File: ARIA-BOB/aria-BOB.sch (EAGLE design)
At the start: 14 parts

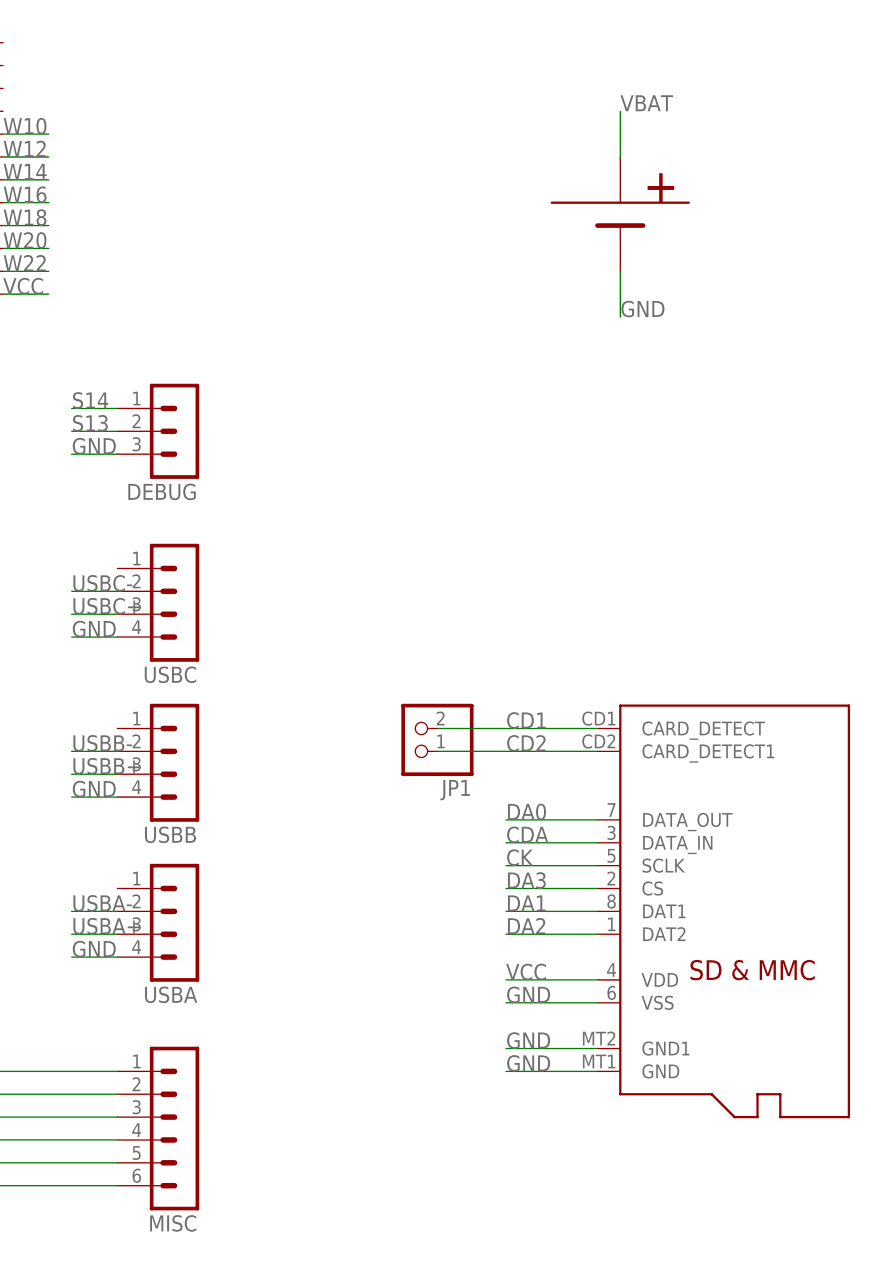
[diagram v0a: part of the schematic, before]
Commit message: SD card footprint aria bob
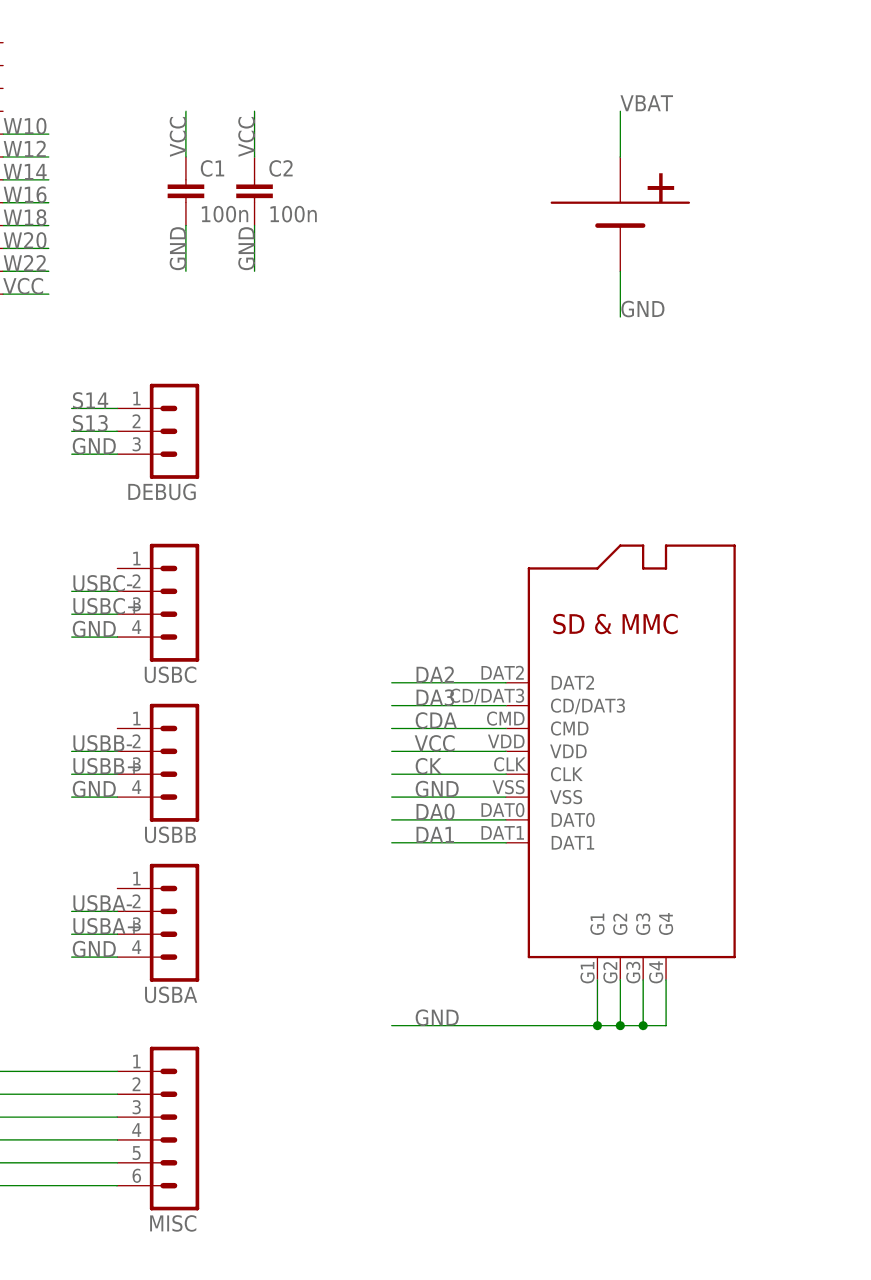
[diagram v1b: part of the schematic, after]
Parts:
- removed JP1: (no value), pinhead:PINHD-1X2
- removed U$2: MICROSD, adafruit:MICROSD
- added C1, C2: 100n, rcl:C-EUC0603
- added U$4: MICRO-SD, octanis-beat:MICRO-SD
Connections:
- removed net CD1: JP1.2, U$2.CARD_DETECT
- removed net CD2: JP1.1, U$2.CARD_DETECT1
- net CDA: now also U$4.CMD; no longer U$2.DATA_IN
- net CK: now also U$4.CLK; no longer U$2.SCLK
- net DA0: now also U$4.DAT0; no longer U$2.DATA_OUT
- net DA1: now also U$4.DAT1; no longer U$2.DAT1
- net DA2: now also U$4.DAT2; no longer U$2.DAT2
- net DA3: now also U$4.CD/DAT3; no longer U$2.CS
- net GND: now also C1.2, C2.2, U$4.G1, U$4.G2, U$4.G3, U$4.G4, U$4.VSS; no longer U$2.GND, U$2.GND1, U$2.VSS
- net VCC: now also C1.1, C2.1, U$4.VDD; no longer U$2.VDD
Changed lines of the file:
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@@
 <part name="MISC" library="con-lstb" deviceset="MA06-1" device=""/>
 <part name="ETH" library="con-lstb" deviceset="MA08-1" device=""/>
-<part name="U$2" library="adafruit" deviceset="MICROSD" device=""/>
-<part name="JP1" library="pinhead" deviceset="PINHD-1X2" device=""/>
 <part name="U$3" library="octanis-beat" deviceset="BAT" device=""/>
 <part name="DEBUG" library="con-lstb" deviceset="MA03-1" device=""/>
+<part name="U$4" library="octanis-beat" deviceset="MICRO-SD" device=""/>
+<part name="C1" library="rcl" deviceset="C-EU" device="C0603" value="100n"/>
+<part name="C2" library="rcl" deviceset="C-EU" device="C0603" value="100n"/>
 </parts>
 <sheets>
@@
 <instance part="MISC" gate="1" x="175.26" y="40.64" rot="R180"/>
 <instance part="ETH" gate="1" x="10.16" y="45.72"/>
-<instance part="U$2" gate="G$1" x="238.76" y="68.58"/>
-<instance part="JP1" gate="G$1" x="200.66" y="86.36" rot="R180"/>
 <instance part="U$3" gate="G$1" x="223.52" y="144.78"/>
 <instance part="DEBUG" gate="G$1" x="175.26" y="119.38" rot="R180"/>
+<instance part="U$4" gate="G$1" x="223.52" y="81.28"/>
+<instance part="C1" gate="G$1" x="175.26" y="147.32"/>
+<instance part="C2" gate="G$1" x="182.88" y="147.32"/>
 </instances>
 <busses>
@@
 </segment>
 <segment>
-<pinref part="U$2" gate="G$1" pin="GND"/>
-<wire x1="220.98" y1="48.26" x2="210.82" y2="48.26" width="0.1524" layer="91"/>
-<label x="210.82" y="48.26" size="1.778" layer="95"/>
-</segment>
-<segment>
-<pinref part="U$2" gate="G$1" pin="GND1"/>
-<wire x1="220.98" y1="50.8" x2="210.82" y2="50.8" width="0.1524" layer="91"/>
-<label x="210.82" y="50.8" size="1.778" layer="95"/>
-</segment>
-<segment>
-<pinref part="U$2" gate="G$1" pin="VSS"/>
-<wire x1="220.98" y1="55.88" x2="210.82" y2="55.88" width="0.1524" layer="91"/>
-<label x="210.82" y="55.88" size="1.778" layer="95"/>
+<wire x1="210.82" y1="78.74" x2="198.12" y2="78.74" width="0.1524" layer="91"/>
+<label x="200.66" y="78.74" size="1.778" layer="95"/>
+<pinref part="U$4" gate="G$1" pin="VSS"/>
 </segment>
 <segment>
@@
 <wire x1="167.64" y1="116.84" x2="162.56" y2="116.84" width="0.1524" layer="91"/>
 <label x="162.56" y="116.84" size="1.778" layer="95"/>
+</segment>
+<segment>
+<pinref part="U$4" gate="G$1" pin="G1"/>
+<wire x1="220.98" y1="58.42" x2="220.98" y2="53.34" width="0.1524" layer="91"/>
+<label x="200.66" y="53.34" size="1.778" layer="95"/>
+<pinref part="U$4" gate="G$1" pin="G2"/>
+<wire x1="220.98" y1="53.34" x2="198.12" y2="53.34" width="0.1524" layer="91"/>
+<wire x1="220.98" y1="53.34" x2="223.52" y2="53.34" width="0.1524" layer="91"/>
+<wire x1="223.52" y1="53.34" x2="223.52" y2="58.42" width="0.1524" layer="91"/>
+<pinref part="U$4" gate="G$1" pin="G3"/>
+<wire x1="226.06" y1="58.42" x2="226.06" y2="53.34" width="0.1524" layer="91"/>
+<wire x1="226.06" y1="53.34" x2="223.52" y2="53.34" width="0.1524" layer="91"/>
+<pinref part="U$4" gate="G$1" pin="G4"/>
+<wire x1="228.6" y1="58.42" x2="228.6" y2="53.34" width="0.1524" layer="91"/>
+<wire x1="228.6" y1="53.34" x2="226.06" y2="53.34" width="0.1524" layer="91"/>
+<junction x="226.06" y="53.34"/>
+<junction x="223.52" y="53.34"/>
+<junction x="220.98" y="53.34"/>
+</segment>
+<segment>
+<pinref part="C1" gate="G$1" pin="2"/>
+<wire x1="175.26" y1="142.24" x2="175.26" y2="137.16" width="0.1524" layer="91"/>
+<label x="175.26" y="137.16" size="1.778" layer="95" rot="R90"/>
+</segment>
+<segment>
+<pinref part="C2" gate="G$1" pin="2"/>
+<wire x1="182.88" y1="142.24" x2="182.88" y2="137.16" width="0.1524" layer="91"/>
+<label x="182.88" y="137.16" size="1.778" layer="95" rot="R90"/>
 </segment>
 </net>
@@
 </segment>
 <segment>
-<pinref part="U$2" gate="G$1" pin="VDD"/>
-<wire x1="220.98" y1="58.42" x2="210.82" y2="58.42" width="0.1524" layer="91"/>
-<label x="210.82" y="58.42" size="1.778" layer="95"/>
+<wire x1="210.82" y1="83.82" x2="198.12" y2="83.82" width="0.1524" layer="91"/>
+<label x="200.66" y="83.82" size="1.778" layer="95"/>
+<pinref part="U$4" gate="G$1" pin="VDD"/>
+</segment>
+<segment>
+<pinref part="C1" gate="G$1" pin="1"/>
+<wire x1="175.26" y1="149.86" x2="175.26" y2="154.94" width="0.1524" layer="91"/>
+<label x="175.26" y="149.86" size="1.778" layer="95" rot="R90"/>
+</segment>
+<segment>
+<pinref part="C2" gate="G$1" pin="1"/>
+<wire x1="182.88" y1="149.86" x2="182.88" y2="154.94" width="0.1524" layer="91"/>
+<label x="182.88" y="149.86" size="1.778" layer="95" rot="R90"/>
 </segment>
 </net>
@@
 </segment>
 <segment>
-<pinref part="U$2" gate="G$1" pin="DATA_OUT"/>
-<wire x1="220.98" y1="76.2" x2="210.82" y2="76.2" width="0.1524" layer="91"/>
-<label x="210.82" y="76.2" size="1.778" layer="95"/>
+<wire x1="210.82" y1="76.2" x2="198.12" y2="76.2" width="0.1524" layer="91"/>
+<label x="200.66" y="76.2" size="1.778" layer="95"/>
+<pinref part="U$4" gate="G$1" pin="DAT0"/>
 </segment>
 </net>
@@
 </segment>
 <segment>
-<pinref part="U$2" gate="G$1" pin="DATA_IN"/>
-<wire x1="220.98" y1="73.66" x2="210.82" y2="73.66" width="0.1524" layer="91"/>
-<label x="210.82" y="73.66" size="1.778" layer="95"/>
+<wire x1="210.82" y1="86.36" x2="198.12" y2="86.36" width="0.1524" layer="91"/>
+<label x="200.66" y="86.36" size="1.778" layer="95"/>
+<pinref part="U$4" gate="G$1" pin="CMD"/>
 </segment>
 </net>
@@
 </segment>
 <segment>
-<pinref part="U$2" gate="G$1" pin="SCLK"/>
-<wire x1="220.98" y1="71.12" x2="210.82" y2="71.12" width="0.1524" layer="91"/>
-<label x="210.82" y="71.12" size="1.778" layer="95"/>
+<wire x1="210.82" y1="81.28" x2="198.12" y2="81.28" width="0.1524" layer="91"/>
+<label x="200.66" y="81.28" size="1.778" layer="95"/>
+<pinref part="U$4" gate="G$1" pin="CLK"/>
 </segment>
 </net>
@@
 </segment>
 <segment>
-<pinref part="U$2" gate="G$1" pin="DAT1"/>
-<wire x1="220.98" y1="66.04" x2="210.82" y2="66.04" width="0.1524" layer="91"/>
-<label x="210.82" y="66.04" size="1.778" layer="95"/>
+<wire x1="210.82" y1="73.66" x2="198.12" y2="73.66" width="0.1524" layer="91"/>
+<label x="200.66" y="73.66" size="1.778" layer="95"/>
+<pinref part="U$4" gate="G$1" pin="DAT1"/>
 </segment>
 </net>
@@
 </segment>
 <segment>
-<pinref part="U$2" gate="G$1" pin="DAT2"/>
-<wire x1="220.98" y1="63.5" x2="210.82" y2="63.5" width="0.1524" layer="91"/>
-<label x="210.82" y="63.5" size="1.778" layer="95"/>
+<wire x1="210.82" y1="91.44" x2="198.12" y2="91.44" width="0.1524" layer="91"/>
+<label x="200.66" y="91.44" size="1.778" layer="95"/>
+<pinref part="U$4" gate="G$1" pin="DAT2"/>
 </segment>
 </net>
@@
 </segment>
 <segment>
-<pinref part="U$2" gate="G$1" pin="CS"/>
-<wire x1="220.98" y1="68.58" x2="210.82" y2="68.58" width="0.1524" layer="91"/>
-<label x="210.82" y="68.58" size="1.778" layer="95"/>
+<wire x1="210.82" y1="88.9" x2="198.12" y2="88.9" width="0.1524" layer="91"/>
+<label x="200.66" y="88.9" size="1.778" layer="95"/>
+<pinref part="U$4" gate="G$1" pin="CD/DAT3"/>
 </segment>
 </net>
@@
 </segment>
 </net>
-<net name="CD2" class="0">
-<segment>
-<pinref part="U$2" gate="G$1" pin="CARD_DETECT1"/>
-<wire x1="220.98" y1="83.82" x2="203.2" y2="83.82" width="0.1524" layer="91"/>
-<label x="210.82" y="83.82" size="1.778" layer="95"/>
-<pinref part="JP1" gate="G$1" pin="1"/>
-</segment>
-</net>
-<net name="CD1" class="0">
-<segment>
-<pinref part="U$2" gate="G$1" pin="CARD_DETECT"/>
-<wire x1="220.98" y1="86.36" x2="203.2" y2="86.36" width="0.1524" layer="91"/>
-<label x="210.82" y="86.36" size="1.778" layer="95"/>
-<pinref part="JP1" gate="G$1" pin="2"/>
-</segment>
-</net>
